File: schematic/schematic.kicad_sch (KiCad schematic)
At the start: 12 parts, among them Q1 PN2222, Q2 PN2222, U1 MCP4161-xxxx-P, U2 MCP4161-xxxx-P, U3 ESP32-WROOM-32E, U4 MCP4161-xxxx-P, U5 MCP4161-xxxx-P

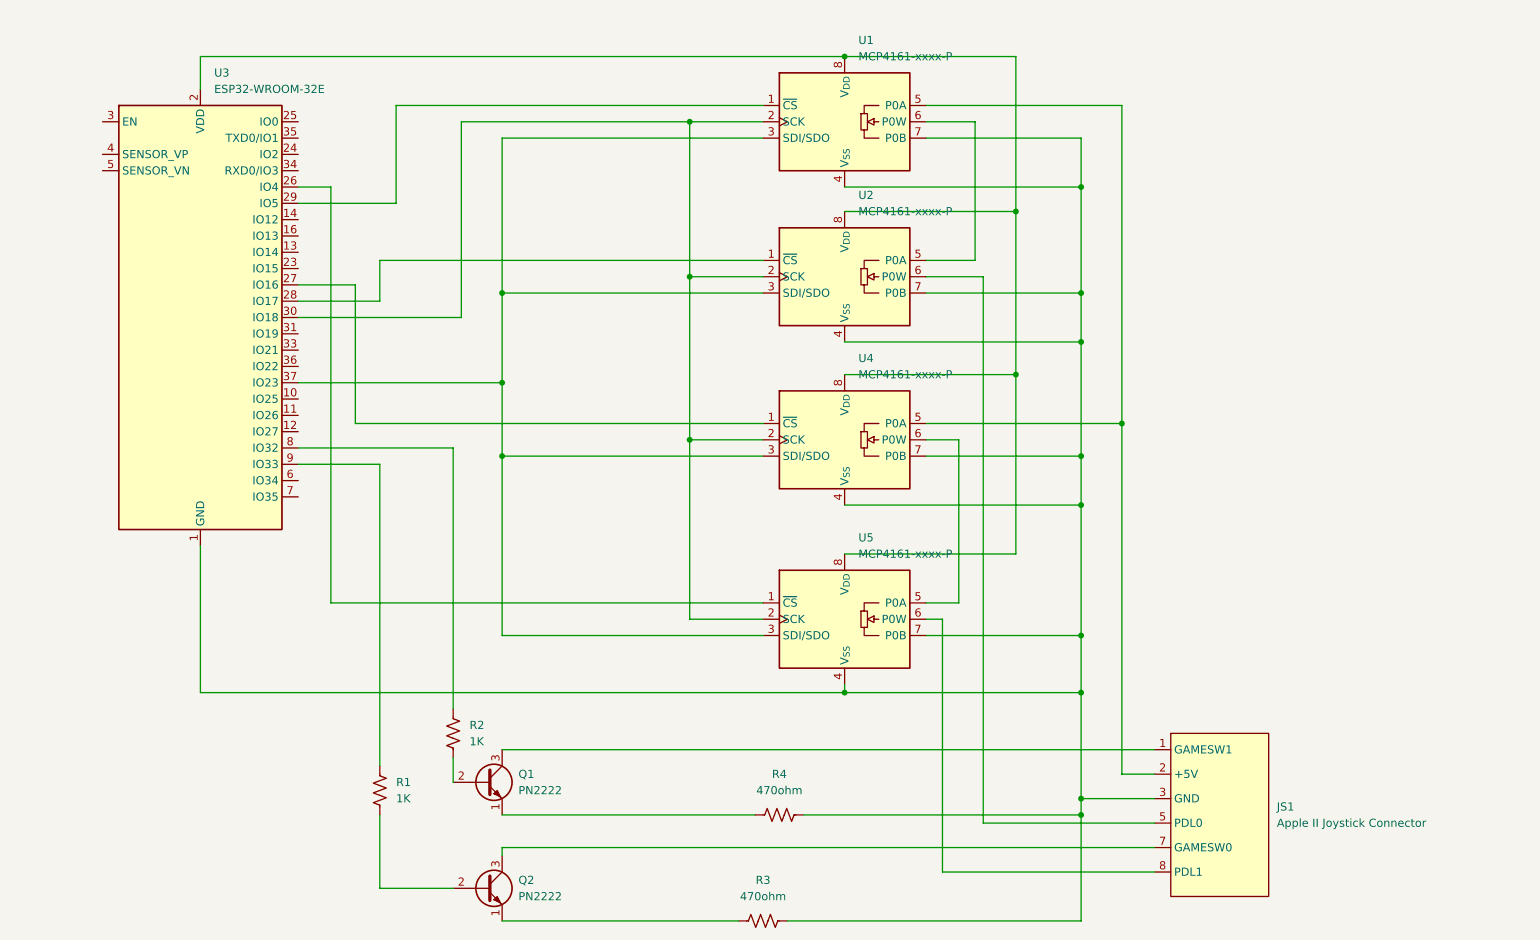
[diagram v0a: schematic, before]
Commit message: modified to use a level shifter between 3.3v and 5v devices.
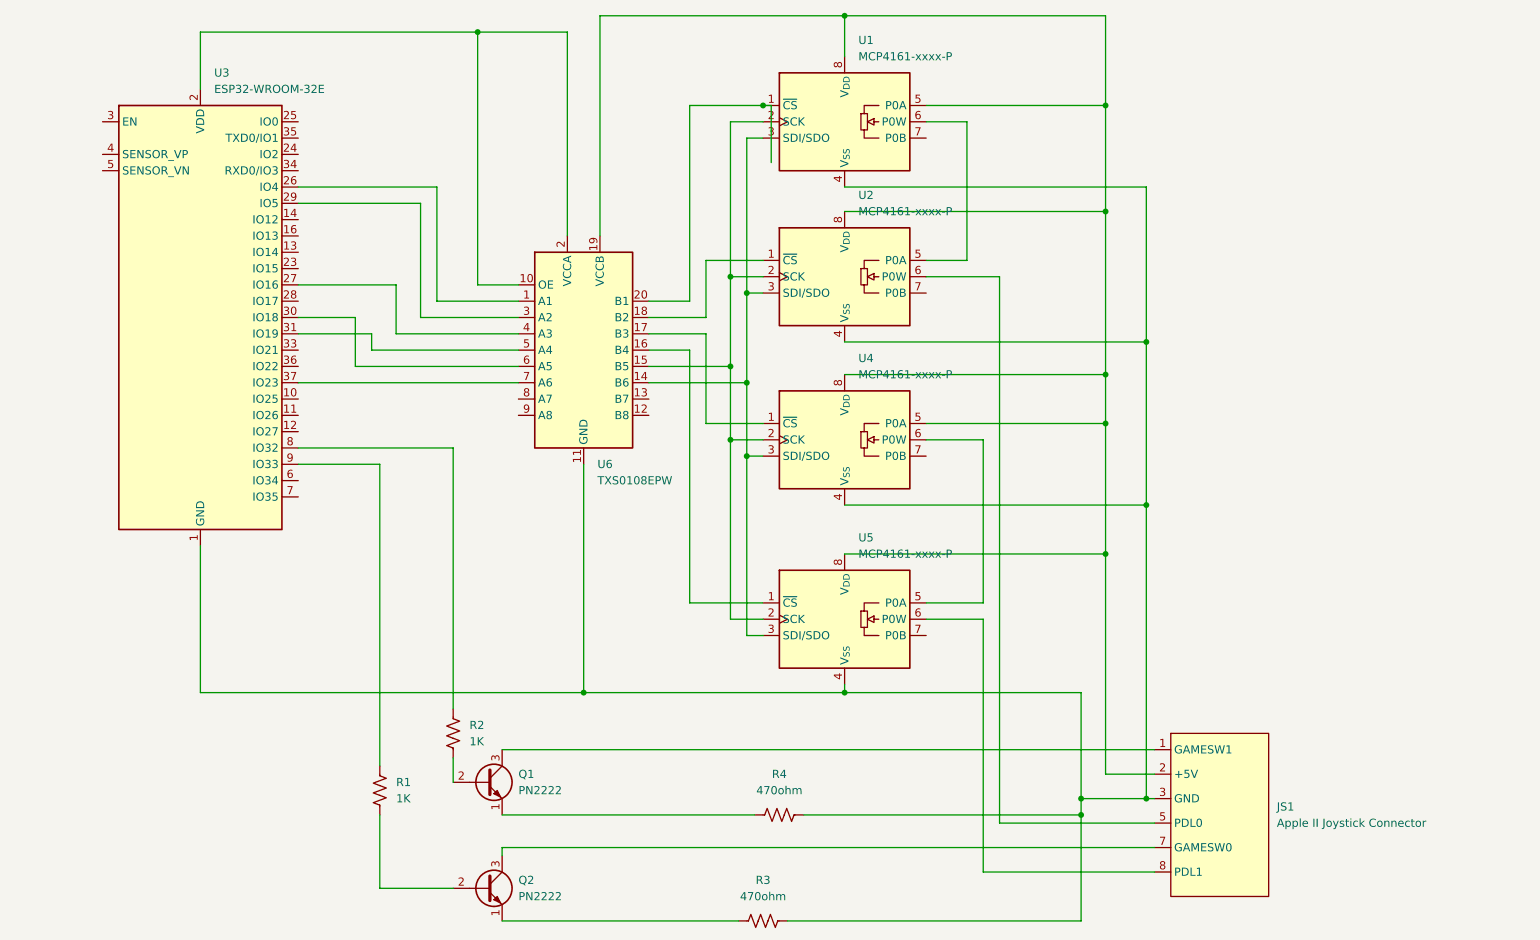
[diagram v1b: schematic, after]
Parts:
- added U6: TXS0108EPW, Package_SO:TSSOP-20_4.4x6.5mm_P0.65mm, symbol Logic_LevelTranslator:TXS0108EPW
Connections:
- net at U1.1 (~{CS}): now also U6.20 (B1); no longer U3.29 (IO5)
- net at U1.2 (SCK), U2.2 (SCK), U4.2 (SCK)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: now also U6.15 (B5); no longer U3.30 (IO18)
- net at U1.3 (SDI/SDO), U2.3 (SDI/SDO), U4.3 (SDI/SDO)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: now also U6.14 (B6); no longer U3.37 (IO23)
- net at JS1.3 (GND), R3.2, R4.2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: now also U6.11 (GND); no longer U1.7 (P0B), U2.7 (P0B), U4.7 (P0B), U5.7 (P0B)
- net at JS1.2 (+5V), U1.5 (P0A), U4.5 (P0A): now also U1.8 (V_{DD}), U2.8 (V_{DD}), U4.8 (V_{DD}), U5.8 (V_{DD}), U6.19 (VCCB)
- net at U4.1 (~{CS}): now also U6.17 (B3); no longer U3.27 (IO16)
- net at U2.1 (~{CS}): now also U6.18 (B2); no longer U3.28 (IO17)
- net at U3.26 (IO4): now also U6.1 (A1); no longer U5.1 (~{CS})
- net at U3.31 (IO19): now also U6.5 (A4)
- new net: U3.2 (VDD), U6.10 (OE), U6.2 (VCCA)
- new net: U5.1 (~{CS}), U6.16 (B4)
- new net: U3.29 (IO5), U6.3 (A2)
- new net: U3.27 (IO16), U6.4 (A3)
- new net: U3.30 (IO18), U6.6 (A5)
- new net: U3.37 (IO23), U6.7 (A6)

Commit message: got analog stick working properly and added basic joystick calibration
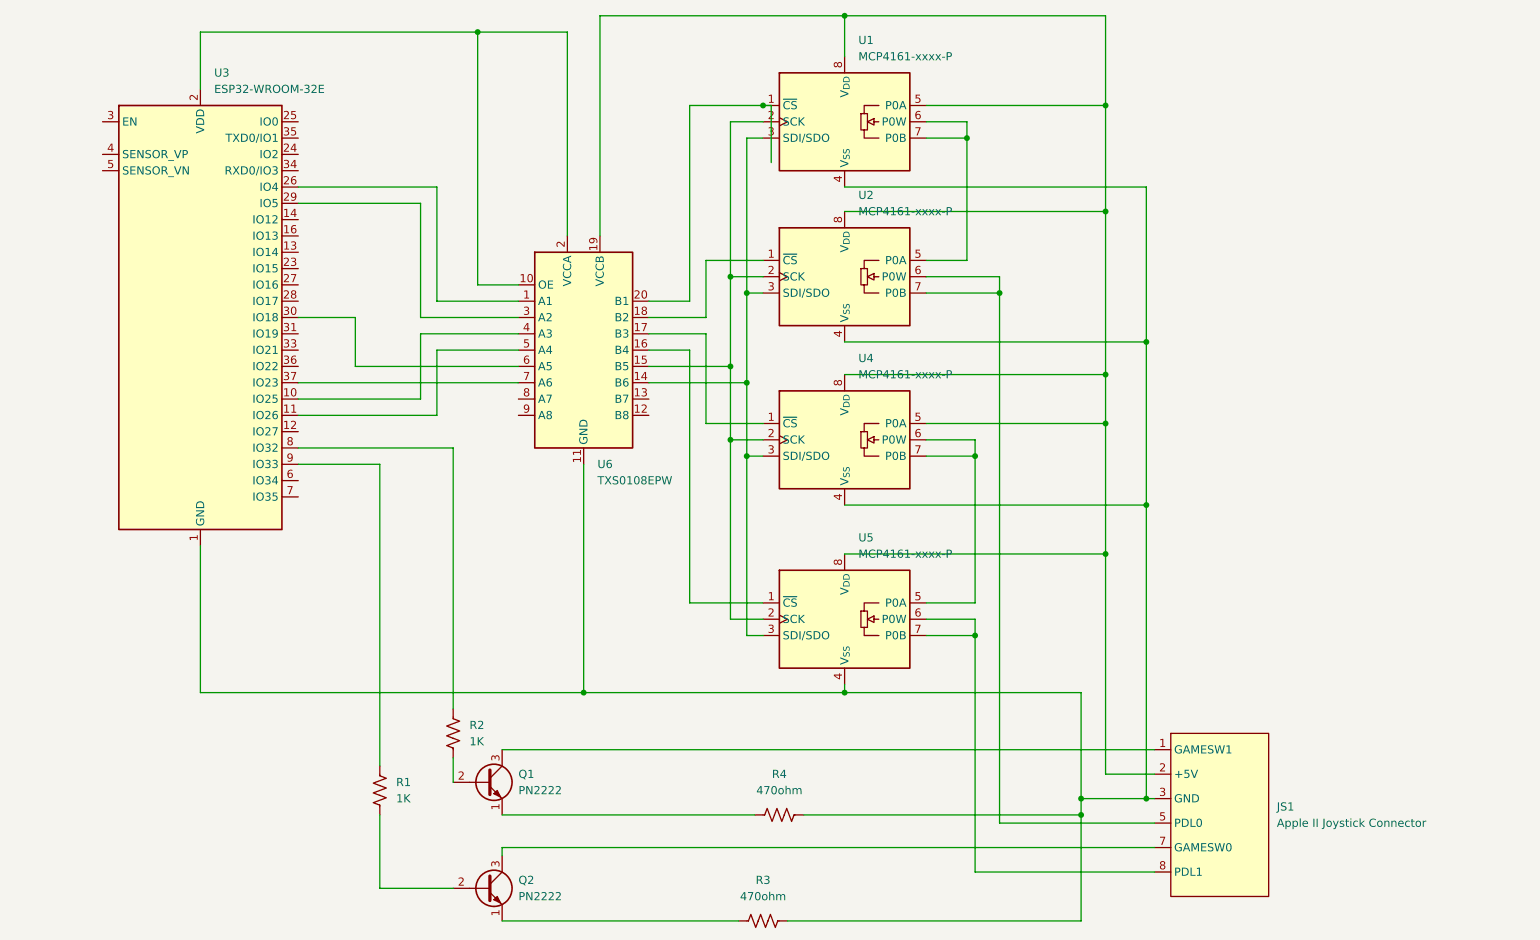
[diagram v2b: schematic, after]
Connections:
- net at U6.4 (A3): now also U3.10 (IO25); no longer U3.27 (IO16)
- net at U6.5 (A4): now also U3.11 (IO26); no longer U3.31 (IO19)
- net at U1.6 (P0W), U2.5 (P0A): now also U1.7 (P0B)
- net at U4.6 (P0W), U5.5 (P0A): now also U4.7 (P0B)
- net at JS1.5 (PDL0), U2.6 (P0W): now also U2.7 (P0B)
- net at JS1.8 (PDL1), U5.6 (P0W): now also U5.7 (P0B)
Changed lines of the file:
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@@
 	(paper "USLetter")
 	(junction
+		(at 171.45 119.38)
+		(diameter 0)
+		(color 0 0 0 0)
+	)
+	(junction
+		(at 170.18 41.91)
+		(diameter 0)
+		(color 0 0 0 0)
+	)
+	(junction
 		(at 198.12 73.66)
 		(diameter 0)
@@
 	)
 	(junction
+		(at 175.26 66.04)
+		(diameter 0)
+		(color 0 0 0 0)
+	)
+	(junction
 		(at 93.98 25.4)
 		(diameter 0)
@@
 	)
 	(junction
+		(at 171.45 91.44)
+		(diameter 0)
+		(color 0 0 0 0)
+	)
+	(junction
 		(at 151.13 128.27)
 		(diameter 0)
@@
 	(wire
 		(pts
+			(xy 170.18 41.91) (xy 170.18 39.37)
+		)
+		(stroke
+			(width 0)
+			(type default)
+		)
+	)
+	(wire
+		(pts
 			(xy 50.8 25.4) (xy 93.98 25.4)
 		)
@@
 	(wire
 		(pts
-			(xy 163.83 114.3) (xy 172.72 114.3)
-		)
-		(stroke
-			(width 0)
-			(type default)
-		)
-	)
-	(wire
-		(pts
-			(xy 66.04 64.77) (xy 81.28 64.77)
+			(xy 163.83 41.91) (xy 170.18 41.91)
 		)
 		(stroke
@@
 	(wire
 		(pts
+			(xy 87.63 74.93) (xy 100.33 74.93)
+		)
+		(stroke
+			(width 0)
+			(type default)
+		)
+	)
+	(wire
+		(pts
 			(xy 74.93 69.85) (xy 74.93 77.47)
 		)
@@
 	(wire
 		(pts
+			(xy 175.26 148.59) (xy 175.26 66.04)
+		)
+		(stroke
+			(width 0)
+			(type default)
+		)
+	)
+	(wire
+		(pts
 			(xy 191.77 22.86) (xy 191.77 36.83)
 		)
@@
 	(wire
 		(pts
+			(xy 163.83 63.5) (xy 175.26 63.5)
+		)
+		(stroke
+			(width 0)
+			(type default)
+		)
+	)
+	(wire
+		(pts
 			(xy 50.8 105.41) (xy 50.8 128.27)
 		)
@@
 	(wire
 		(pts
+			(xy 85.09 82.55) (xy 85.09 72.39)
+		)
+		(stroke
+			(width 0)
+			(type default)
+		)
+	)
+	(wire
+		(pts
 			(xy 120.65 67.31) (xy 127 67.31)
 		)
@@
 	(wire
 		(pts
+			(xy 199.39 156.21) (xy 171.45 156.21)
+		)
+		(stroke
+			(width 0)
+			(type default)
+		)
+	)
+	(wire
+		(pts
 			(xy 113.03 22.86) (xy 151.13 22.86)
 		)
@@
 	(wire
 		(pts
-			(xy 163.83 63.5) (xy 175.26 63.5)
+			(xy 87.63 85.09) (xy 87.63 74.93)
 		)
 		(stroke
@@
 	(wire
 		(pts
-			(xy 66.04 72.39) (xy 77.47 72.39)
-		)
-		(stroke
-			(width 0)
-			(type default)
-		)
-	)
-	(wire
-		(pts
 			(xy 66.04 90.17) (xy 90.17 90.17)
 		)
@@
 	(wire
 		(pts
-			(xy 170.18 60.96) (xy 163.83 60.96)
-		)
-		(stroke
-			(width 0)
-			(type default)
-		)
-	)
-	(wire
-		(pts
 			(xy 97.79 152.4) (xy 97.79 153.67)
 		)
@@
 	(wire
 		(pts
-			(xy 170.18 39.37) (xy 170.18 60.96)
-		)
-		(stroke
-			(width 0)
-			(type default)
-		)
-	)
-	(wire
-		(pts
-			(xy 81.28 64.77) (xy 81.28 72.39)
+			(xy 175.26 63.5) (xy 175.26 66.04)
 		)
 		(stroke
@@
 	(wire
 		(pts
-			(xy 172.72 116.84) (xy 172.72 156.21)
+			(xy 171.45 91.44) (xy 163.83 91.44)
 		)
 		(stroke
@@
 	(wire
 		(pts
+			(xy 171.45 119.38) (xy 163.83 119.38)
+		)
+		(stroke
+			(width 0)
+			(type default)
+		)
+	)
+	(wire
+		(pts
+			(xy 163.83 60.96) (xy 170.18 60.96)
+		)
+		(stroke
+			(width 0)
+			(type default)
+		)
+	)
+	(wire
+		(pts
 			(xy 133.35 77.47) (xy 133.35 63.5)
 		)
@@
 	(wire
 		(pts
+			(xy 171.45 116.84) (xy 171.45 119.38)
+		)
+		(stroke
+			(width 0)
+			(type default)
+		)
+	)
+	(wire
+		(pts
+			(xy 171.45 88.9) (xy 171.45 91.44)
+		)
+		(stroke
+			(width 0)
+			(type default)
+		)
+	)
+	(wire
+		(pts
 			(xy 142.24 163.83) (xy 187.96 163.83)
 		)
@@
 	(wire
 		(pts
+			(xy 171.45 156.21) (xy 171.45 119.38)
+		)
+		(stroke
+			(width 0)
+			(type default)
+		)
+	)
+	(wire
+		(pts
 			(xy 199.39 152.4) (xy 97.79 152.4)
 		)
@@
 	(wire
 		(pts
+			(xy 163.83 116.84) (xy 171.45 116.84)
+		)
+		(stroke
+			(width 0)
+			(type default)
+		)
+	)
+	(wire
+		(pts
 			(xy 133.35 116.84) (xy 133.35 88.9)
 		)
@@
 	(wire
 		(pts
+			(xy 163.83 114.3) (xy 171.45 114.3)
+		)
+		(stroke
+			(width 0)
+			(type default)
+		)
+	)
+	(wire
+		(pts
 			(xy 97.79 137.16) (xy 199.39 137.16)
 		)
@@
 	(wire
 		(pts
+			(xy 66.04 82.55) (xy 85.09 82.55)
+		)
+		(stroke
+			(width 0)
+			(type default)
+		)
+	)
+	(wire
+		(pts
+			(xy 170.18 60.96) (xy 170.18 41.91)
+		)
+		(stroke
+			(width 0)
+			(type default)
+		)
+	)
+	(wire
+		(pts
 			(xy 151.13 49.53) (xy 198.12 49.53)
 		)
@@
 	(wire
 		(pts
-			(xy 172.72 156.21) (xy 199.39 156.21)
-		)
-		(stroke
-			(width 0)
-			(type default)
-		)
-	)
-	(wire
-		(pts
 			(xy 78.74 158.75) (xy 90.17 158.75)
 		)
@@
 	(wire
 		(pts
-			(xy 163.83 88.9) (xy 172.72 88.9)
-		)
-		(stroke
-			(width 0)
-			(type default)
-		)
-	)
-	(wire
-		(pts
 			(xy 151.13 73.66) (xy 198.12 73.66)
 		)
@@
 	(wire
 		(pts
-			(xy 175.26 63.5) (xy 175.26 148.59)
-		)
-		(stroke
-			(width 0)
-			(type default)
-		)
-	)
-	(wire
-		(pts
-			(xy 77.47 74.93) (xy 100.33 74.93)
+			(xy 163.83 66.04) (xy 175.26 66.04)
 		)
 		(stroke
@@
 	(wire
 		(pts
-			(xy 81.28 72.39) (xy 100.33 72.39)
-		)
-		(stroke
-			(width 0)
-			(type default)
-		)
-	)
-	(wire
-		(pts
 			(xy 151.13 128.27) (xy 187.96 128.27)
 		)
@@
 	(wire
 		(pts
+			(xy 171.45 114.3) (xy 171.45 91.44)
+		)
+		(stroke
+			(width 0)
+			(type default)
+		)
+	)
+	(wire
+		(pts
+			(xy 66.04 85.09) (xy 87.63 85.09)
+		)
+		(stroke
+			(width 0)
+			(type default)
+		)
+	)
+	(wire
+		(pts
 			(xy 127 74.93) (xy 127 114.3)
 		)
@@
 	(wire
 		(pts
-			(xy 172.72 88.9) (xy 172.72 114.3)
-		)
-		(stroke
-			(width 0)
-			(type default)
-		)
-	)
-	(wire
-		(pts
 			(xy 85.09 52.07) (xy 85.09 69.85)
 		)
@@
 	(wire
 		(pts
+			(xy 163.83 88.9) (xy 171.45 88.9)
+		)
+		(stroke
+			(width 0)
+			(type default)
+		)
+	)
+	(wire
+		(pts
 			(xy 144.78 147.32) (xy 187.96 147.32)
 		)
@@
 	(wire
 		(pts
-			(xy 163.83 116.84) (xy 172.72 116.84)
-		)
-		(stroke
-			(width 0)
-			(type default)
-		)
-	)
-	(wire
-		(pts
 			(xy 87.63 67.31) (xy 100.33 67.31)
 		)
@@
 	(wire
 		(pts
-			(xy 77.47 72.39) (xy 77.47 74.93)
-		)
-		(stroke
+			(xy 85.09 72.39) (xy 100.33 72.39)
+		)
+		(stroke

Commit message: updated to actually work, end-to-end
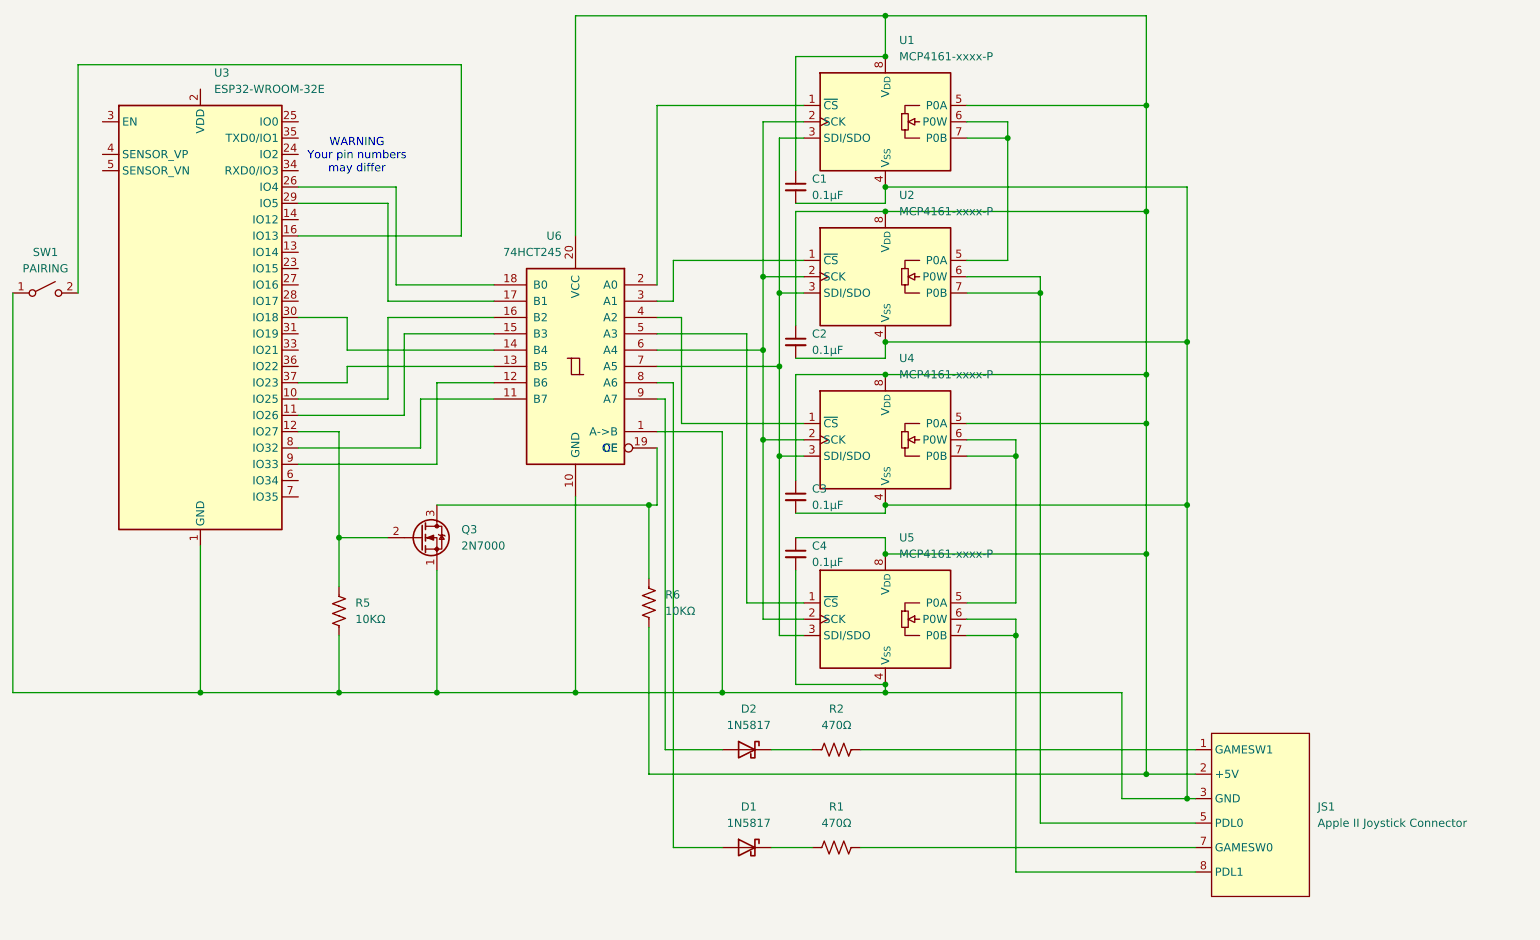
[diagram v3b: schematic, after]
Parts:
- removed Q1, Q2: PN2222, Package_TO_SOT_THT:TO-92_Inline, symbol Transistor_BJT:PN2222A
- removed R3, R4: 470ohm, symbol Device:R_US
- removed U6: TXS0108EPW, Package_SO:TSSOP-20_4.4x6.5mm_P0.65mm, symbol Logic_LevelTranslator:TXS0108EPW
- added C1, C2, C3, C4: 0.1µF, symbol Device:C_Small
- added D1, D2: 1N5817, Diode_THT:D_DO-41_SOD81_P10.16mm_Horizontal, symbol Diode:1N5817
- added Q3: 2N7000, Package_TO_SOT_THT:TO-92_Inline, symbol Transistor_FET:2N7000
- added R5, R6: 10KΩ, symbol Device:R_US
- added SW1: PAIRING, symbol Switch:SW_SPST
- added U6: 74HCT245, symbol 74xx:74HC245
- R1, R2: value 1K -> 470Ω
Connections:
- net at U3.26 (IO4): now also U6.18 (B0)
- net at JS1.3 (GND), U1.4 (V_{SS}), U2.4 (V_{SS})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: now also C1.2, C2.2, C3.2, C4.2, Q3.1 (S), R5.2, SW1.1 (A), U6.1 (A->B), U6.10 (GND)
- net at U1.3 (SDI/SDO), U2.3 (SDI/SDO), U4.3 (SDI/SDO)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: now also U6.7 (A5)
- net at U1.2 (SCK), U2.2 (SCK), U4.2 (SCK)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: now also U6.6 (A4)
- net at U5.1 (~{CS}): now also U6.5 (A3)
- net at U4.1 (~{CS}): now also U6.4 (A2)
- net at U2.1 (~{CS}): now also U6.3 (A1)
- net at JS1.2 (+5V), U1.5 (P0A), U1.8 (V_{DD})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: now also C1.1, C2.1, C3.1, C4.1, R6.2, U6.20 (VCC)
- net at U1.1 (~{CS}): now also U6.2 (A0)
- net at U3.29 (IO5): now also U6.17 (B1)
- net at U3.10 (IO25): now also U6.16 (B2)
- net at U3.11 (IO26): now also U6.15 (B3)
- net at U3.30 (IO18): now also U6.14 (B4)
- net at U3.37 (IO23): now also U6.13 (B5)
- net at R2.2: now also JS1.1 (GAMESW1)
- net at U3.8 (IO32): now also U6.11 (B7); no longer R2.1
- net at R1.2: now also JS1.7 (GAMESW0)
- net at R1.1: now also D1.1 (K); no longer U3.9 (IO33)
- net at U3.12 (IO27): now also Q3.2 (G), R5.1
- net at U3.16 (IO13): now also SW1.2 (B)
- new net: D1.2 (A), U6.8 (A6)
- new net: U3.9 (IO33), U6.12 (B6)
- new net: Q3.3 (D), R6.1, U6.19 (CE)
- new net: D2.2 (A), U6.9 (A7)
- new net: D2.1 (K), R2.1
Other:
- note added: "OE"
- note added: "WARNING Your pin numbers may differ"
- moved on the sheet: JS1, U1, U2, U4, U5
